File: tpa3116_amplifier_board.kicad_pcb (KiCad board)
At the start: 2 copper layers, 62.2 x 50.8 mm, 43 parts, among them IC1 TPA3116D2QDADRQ1, J1 control, J2 Conn_01x02, J3 output_right, J4 power_supply, J5 power_supply

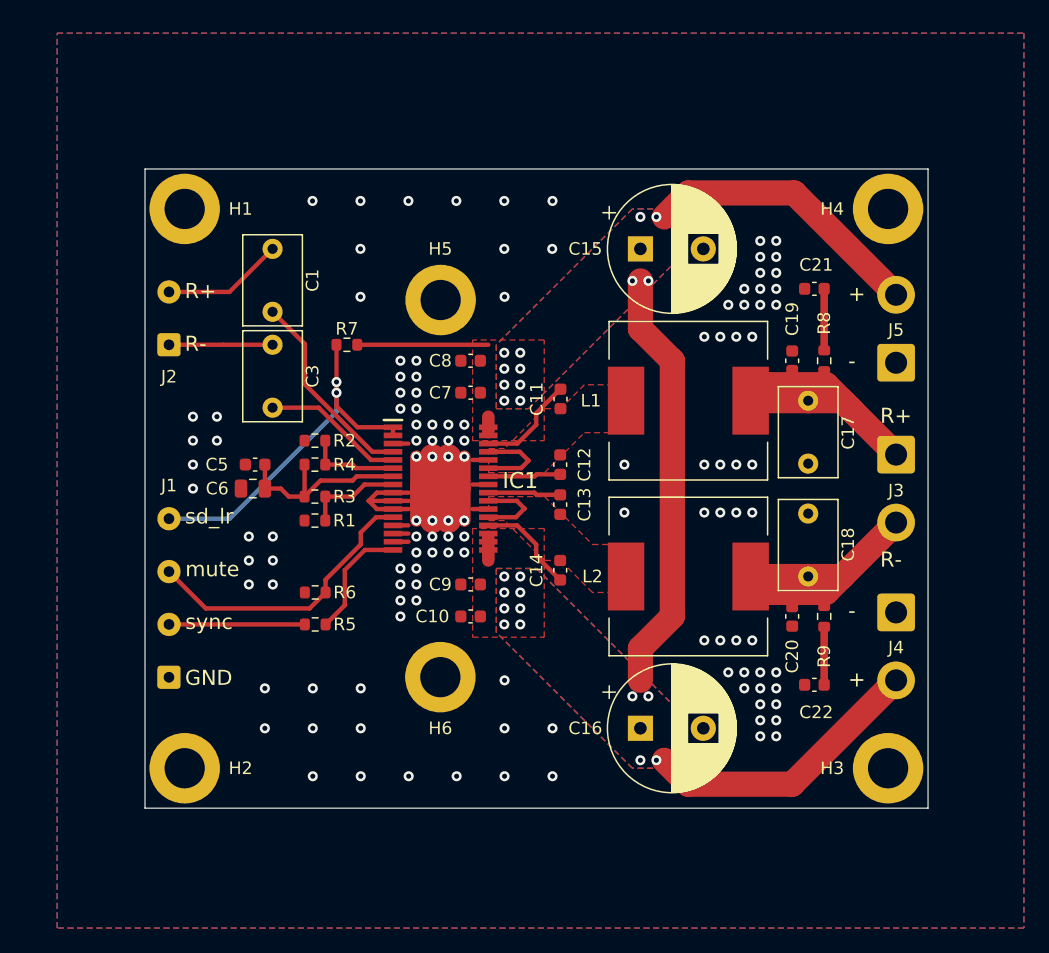
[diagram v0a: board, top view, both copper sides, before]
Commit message: Заменил пленочные выводные конденсаторы в фильтре на SMD
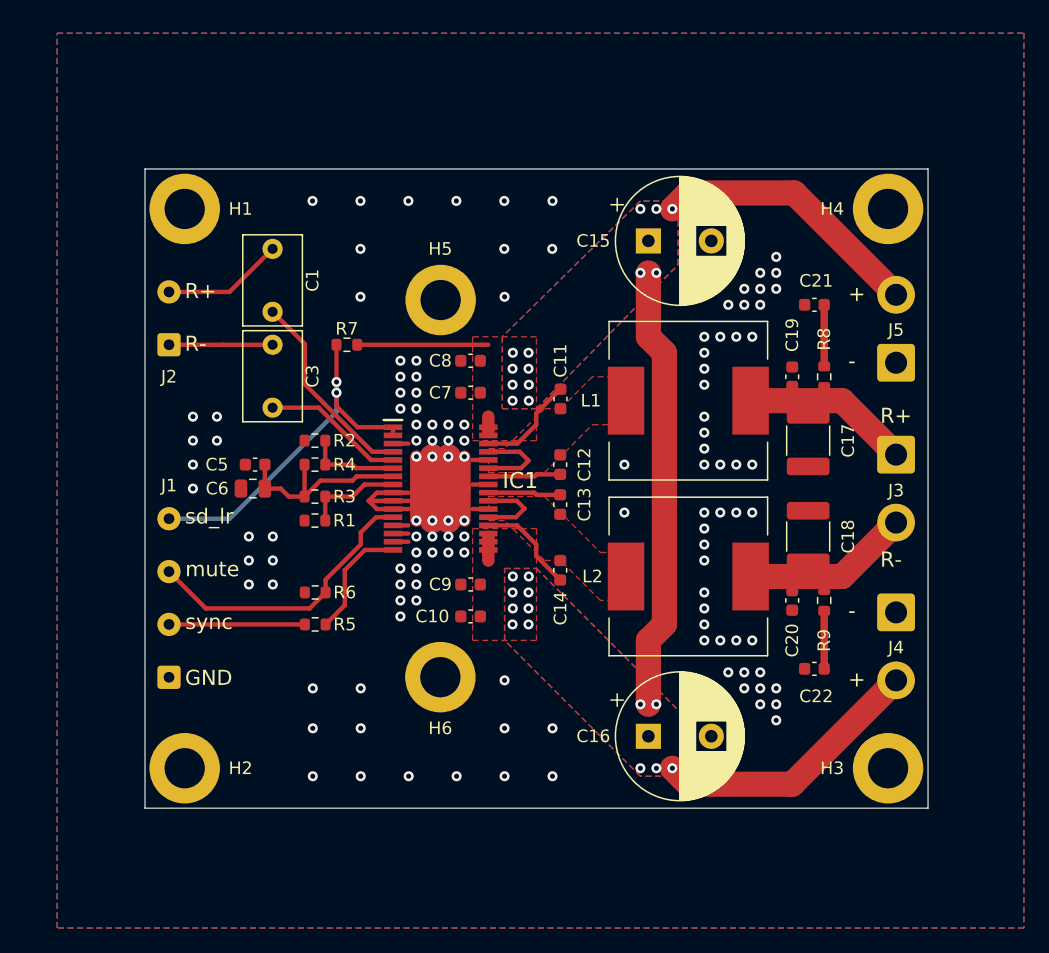
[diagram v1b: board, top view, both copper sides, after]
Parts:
- C17, C18: footprint Capacitor_THT:C_Rect_L7.0mm_W4.5mm_P5.00mm -> Capacitor_SMD:C_1812_4532Metric
- L1, L2: value 22u -> 10u
- moved C18 3.17 mm to (153.7, 123.8)
- moved C17 1.83 mm to (153.7, 116.2)
- moved C20 1.27 mm to (152.4, 128.9)
- moved C22 1.27 mm to (154.2, 134.3)
- moved R9 1.27 mm to (154.9, 128.9)
- moved C19 1.27 mm to (152.4, 111.1)
- moved C21 1.27 mm to (154.2, 105.4)
- moved R8 1.27 mm to (154.9, 111.1)
- moved C15 0.90 mm to (141.0, 100.3)
- moved C16 0.90 mm to (141.0, 139.7)
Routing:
- net Net-(J3-Pin_1): track 22.9 -> 13.3 mm
- net Net-(J3-Pin_2): track 22.0 -> 13.8 mm
- net VCC: track 92.5 -> 92.2 mm, vias 24 -> 26
- net GND: vias 121 -> 123

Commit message: Уменьшил размер платы
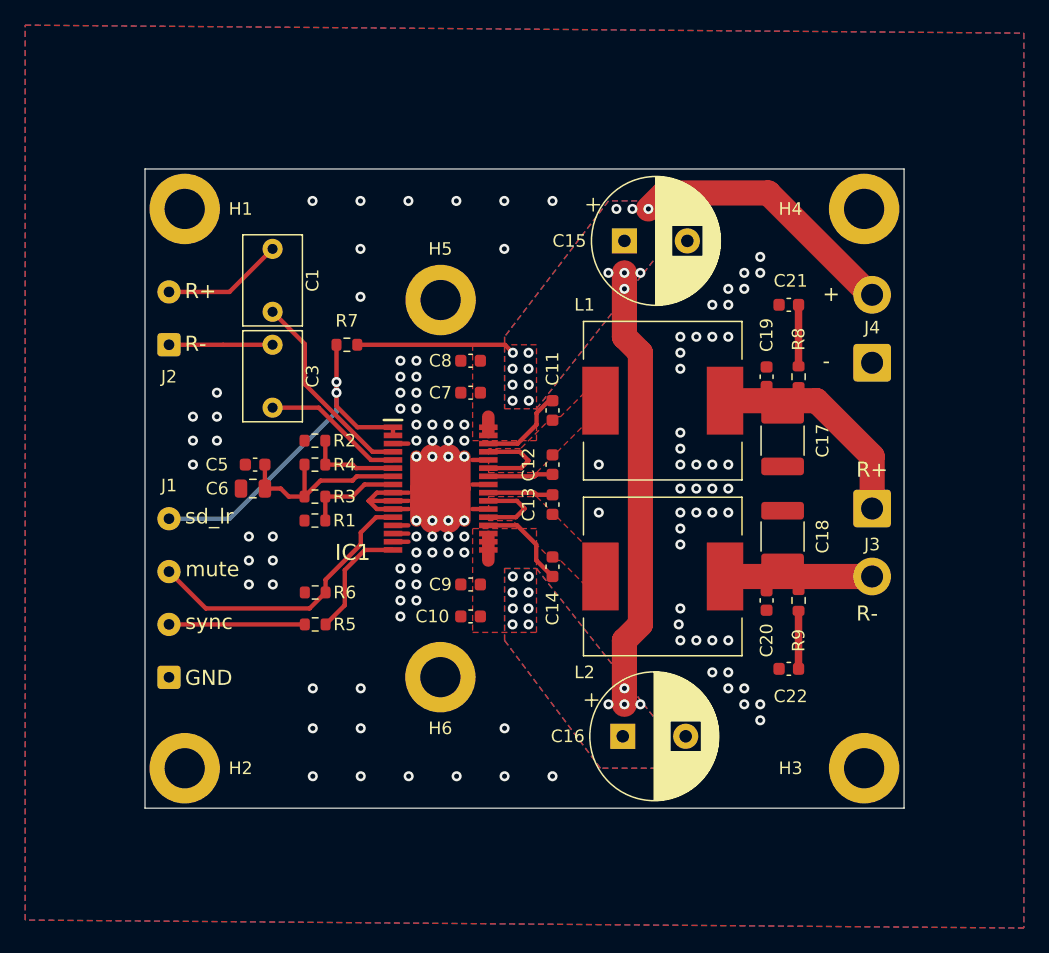
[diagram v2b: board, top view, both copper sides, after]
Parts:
- removed J5: power_supply, Connector_Wire:SolderWire-1sqmm_1x02_P5.4mm_D1.4mm_OD2.7mm
- moved J4 19.9 mm to (158.8, 110.0), turned to 90 degrees
- moved J3 4.69 mm to (158.8, 121.6)
- moved C16 2.03 mm to (138.9, 139.7)
- moved C17 2.03 mm to (151.6, 116.2)
- moved C18 2.03 mm to (151.6, 123.8)
- moved C19 2.03 mm to (150.4, 111.1)
- moved C20 2.03 mm to (150.4, 128.9)
- moved C21 2.03 mm to (152.1, 105.4)
- moved C22 2.03 mm to (152.1, 134.3)
- moved L1 2.03 mm to (142.1, 113.0)
- moved L2 2.03 mm to (142.1, 127.0)
- moved R8 2.03 mm to (152.9, 111.1)
- moved R9 2.03 mm to (152.9, 128.9)
- moved C15 1.91 mm to (139.1, 100.3)
- moved H3 1.91 mm to (158.1, 142.2)
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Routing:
- net VCC: track 92.2 -> 72.6 mm, vias 26 -> 27
- net Net-(J3-Pin_1): track 13.3 -> 17.7 mm
- net Net-(J3-Pin_2): track 13.8 -> 12.2 mm
- net Net-(IC1-BSPR): track 8.04 -> 7.17 mm
- net Net-(IC1-BSPL): track 5.79 -> 5.17 mm
- net Net-(IC1-BSNR): track 5.78 -> 5.17 mm
- net Net-(IC1-BSNL): track 8.05 -> 7.51 mm
- net GND: vias 123 -> 115
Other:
- board size 62.2 x 50.8 mm -> 60.3 x 50.8 mm

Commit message: Уменьшил размер коннекторов и подправил переходные отверстия
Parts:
- J3, J4: footprint Connector_Wire:SolderWire-1sqmm_1x02_P5.4mm_D1.4mm_OD2.7mm -> Connector_Wire:SolderWire-0.75sqmm_1x02_P4.8mm_D1.25mm_OD2.3mm
- moved J3 0.60 mm to (158.8, 122.2)
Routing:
- net GND: track 39.7 -> 45.4 mm, vias 115 -> 121
- net Net-(J3-Pin_1): track 17.7 -> 18.3 mm

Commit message: Небольшие правки
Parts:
- C1, C3: footprint Capacitor_THT:C_Rect_L7.0mm_W4.5mm_P5.00mm -> Capacitor_THT:C_Rect_L7.0mm_W6.0mm_P5.00mm
- moved R7 1.74 mm to (118.7, 108.6)
- moved C3 0.62 mm to (110.5, 108.7)
- moved C1 0.61 mm to (110.5, 101.0)
- moved C5 0.32 mm to (109.7, 118.4)
- moved C6 0.32 mm to (109.5, 120.3)
- moved R1 0.32 mm to (114.5, 122.9)
- moved R2 0.32 mm to (114.5, 116.5)
- moved R3 0.32 mm to (114.5, 121.0)
- moved R4 0.32 mm to (114.5, 118.4)
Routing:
- net VCC: track 73.0 -> 71.2 mm
- net /SD_LR: track 29.9 -> 30.7 mm
- net /R+: track 9.65 -> 9.04 mm
- net Net-(IC1-RINN): track 11.3 -> 11.9 mm
- net /R-: track 8.25 -> 7.64 mm
- net GND: vias 121 -> 115

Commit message: Небольшие правки
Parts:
- removed C20: 1n, Capacitor_SMD:C_0603_1608Metric
- removed C21, C22: 10n, Capacitor_SMD:C_0603_1608Metric
- added C2: 470n, Capacitor_THT:C_Rect_L7.0mm_W4.5mm_P5.00mm, F.Cu at (110.7, 109.3)
- added C4: 1n, Capacitor_SMD:C_0603_1608Metric, F.Cu at (126.9, 127.6)
- C1: footprint Capacitor_THT:C_Rect_L7.0mm_W6.0mm_P5.00mm -> Capacitor_THT:C_Rect_L7.0mm_W4.5mm_P5.00mm
- C12, C13: value 220n -> 35v 470u; footprint Capacitor_SMD:C_0603_1608Metric -> Capacitor_THT:CP_Radial_D10.0mm_P5.00mm
- C14: value 220n -> 470n; footprint Capacitor_SMD:C_0603_1608Metric -> Capacitor_SMD:C_1812_4532Metric
- C15: value 35v 470u -> 470n; footprint Capacitor_THT:CP_Radial_D10.0mm_P5.00mm -> Capacitor_SMD:C_1812_4532Metric
- C16: value 35v 470u -> 1n; footprint Capacitor_THT:CP_Radial_D10.0mm_P5.00mm -> Capacitor_SMD:C_0603_1608Metric
- C17: value 470n -> 1n; footprint Capacitor_SMD:C_1812_4532Metric -> Capacitor_SMD:C_0603_1608Metric
- C18: value 470n -> 10n; footprint Capacitor_SMD:C_1812_4532Metric -> Capacitor_SMD:C_0603_1608Metric
- C19: value 1n -> 10n
- C3: value 470n -> 1u; footprint Capacitor_THT:C_Rect_L7.0mm_W6.0mm_P5.00mm -> Capacitor_SMD:C_0805_2012Metric
- C5: value -- -> 1n
- C6: value 1u -> 220n; footprint Capacitor_SMD:C_0805_2012Metric -> Capacitor_SMD:C_0603_1608Metric
- C7, C8: value 1n -> 220n
- J1: value control -> power_supply; footprint Connector_Wire:SolderWire-0.25sqmm_1x04_P4.2mm_D0.65mm_OD1.7mm -> Connector_Wire:SolderWire-0.25sqmm_1x02_P4.2mm_D0.65mm_OD1.7mm
- J2: value Conn_01x02 -> Conn_01x04; footprint Connector_Wire:SolderWire-0.25sqmm_1x02_P4.2mm_D0.65mm_OD1.7mm -> Connector_Wire:SolderWire-0.25sqmm_1x04_P4.2mm_D0.65mm_OD1.7mm
- J3: value output_right -> power_supply
- J4: value power_supply -> output_right
- moved C16 30.8 mm to (150.5, 111.1), turned to -90 degrees
- moved C15 26.7 mm to (151.8, 123.8), turned to 90 degrees
- moved J2 25.4 mm to (102.9, 134.0)
- moved J1 24.8 mm to (102.9, 110.2)
- moved C14 21.0 mm to (151.8, 116.2), turned to 90 degrees
- moved C6 19.9 mm to (126.9, 130.2), turned to 180 degrees
- moved C13 19.3 mm to (139.1, 139.7), turned to 0 degrees
- moved C12 18.7 mm to (139.1, 100.3), turned to 0 degrees
- moved C5 18.2 mm to (126.9, 112.4)
- moved C19 18.0 mm to (153.0, 128.9)
- moved C18 12.8 mm to (153.0, 111.1)
- moved C17 12.8 mm to (150.5, 128.9), turned to -90 degrees
- moved C11 12.4 mm to (133.3, 126.2), turned to -90 degrees
- moved J3 12.3 mm to (158.8, 109.9), turned to 90 degrees
- moved C3 12.3 mm to (110.5, 121.0), turned to 90 degrees
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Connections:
- C10 pad 1: VCC -> Net-(IC1-OUTNL)
- C10 pad 2: GND -> Net-(IC1-BSPL)
- C11 pad 1: Net-(IC1-OUTNR) -> Net-(IC1-OUTNL)
- C11 pad 2: Net-(IC1-BSPR) -> Net-(IC1-BSNL)
- C12 pad 1: Net-(IC1-OUTNR) -> VCC
- C12 pad 2: Net-(IC1-BSNR) -> GND
- C13 pad 1: Net-(IC1-OUTNL) -> VCC
- C13 pad 2: Net-(IC1-BSPL) -> GND
- C14 pad 1: Net-(IC1-OUTNL) -> GND
- C14 pad 2: Net-(IC1-BSNL) -> Net-(J4-Pin_1)
- C15 pad 1: VCC -> Net-(J4-Pin_2)
- C16 pad 1: VCC -> GND
- C16 pad 2: GND -> Net-(J4-Pin_1)
- C17 pad 1: GND -> Net-(J4-Pin_2)
- C17 pad 2: Net-(J3-Pin_1) -> GND
- C18 pad 1: Net-(J3-Pin_2) -> Net-(J4-Pin_1)
- C18 pad 2: GND -> Net-(C18-Pad2)
- C19 pad 1: GND -> Net-(J4-Pin_2)
- C19 pad 2: Net-(J3-Pin_1) -> Net-(C19-Pad2)
- C3 pad 1: /R- -> GND
- C3 pad 2: Net-(IC1-RINN) -> Net-(IC1-GVDD)
- C5 pad 2: Net-(IC1-GVDD) -> VCC
- C6 pad 1: GND -> VCC
- C6 pad 2: Net-(IC1-GVDD) -> GND
- C8 pad 1: GND -> Net-(IC1-OUTNR)
- C8 pad 2: VCC -> Net-(IC1-BSPR)
- C9 pad 1: VCC -> Net-(IC1-OUTNR)
- C9 pad 2: GND -> Net-(IC1-BSNR)
- J1 pad 1: GND -> /R-
- J1 pad 2: /sync -> /R+
- J2 pad 1: /R- -> GND
- J2 pad 2: /R+ -> /sync
- J3 pad 1: Net-(J3-Pin_1) -> GND
- J3 pad 2: Net-(J3-Pin_2) -> VCC
- J4 pad 1: GND -> Net-(J4-Pin_1)
- J4 pad 2: VCC -> Net-(J4-Pin_2)
- L1 pad 2: Net-(J3-Pin_1) -> Net-(J4-Pin_1)
- L2 pad 2: Net-(J3-Pin_2) -> Net-(J4-Pin_2)
- R8 pad 1: Net-(J3-Pin_1) -> GND
- R8 pad 2: Net-(C21-Pad2) -> Net-(C18-Pad2)
- R9 pad 1: Net-(J3-Pin_2) -> GND
- R9 pad 2: Net-(C22-Pad2) -> Net-(C19-Pad2)
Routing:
- net Net-(J4-Pin_1): track 0.00 -> 18.3 mm
- net Net-(J3-Pin_1): track 18.3 -> 0.00 mm
- net Net-(J3-Pin_2): track 12.2 -> 0.00 mm
- net Net-(J4-Pin_2): track 0.00 -> 11.7 mm
- net GND: track 45.4 -> 35.0 mm, vias 115 -> 93
- net Net-(C19-Pad2): track 0.00 -> 4.94 mm
- net Net-(C18-Pad2): track 0.00 -> 4.94 mm
- net Net-(C22-Pad2): track 4.61 -> 0.00 mm
- net Net-(C21-Pad2): track 4.42 -> 0.00 mm
- net Net-(IC1-GVDD): track 15.7 -> 14.2 mm
- net Net-(IC1-RINP): track 16.3 -> 15.2 mm
- net Net-(IC1-PLIMIT): track 7.25 -> 8.27 mm
- net Net-(IC1-GAIN/SLV): track 7.81 -> 8.79 mm
- net /SD_LR: track 30.7 -> 29.8 mm
- net /R+: track 9.04 -> 9.68 mm
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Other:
- board text added: "fault"
- board text removed: "sd_lr"
